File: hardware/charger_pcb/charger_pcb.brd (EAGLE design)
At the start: 60 x 30 mm, 17 parts

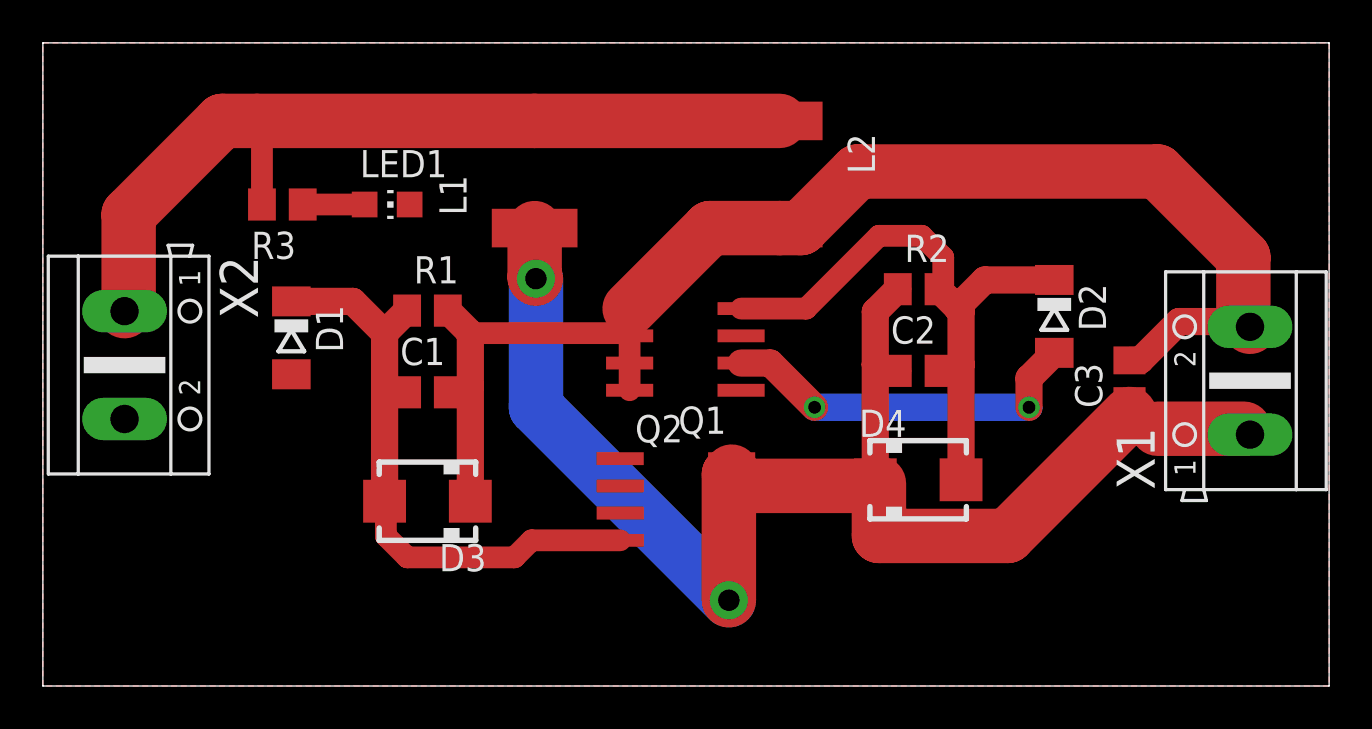
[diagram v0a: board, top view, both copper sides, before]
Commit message: better dir struct, and some tweaks to pcbs
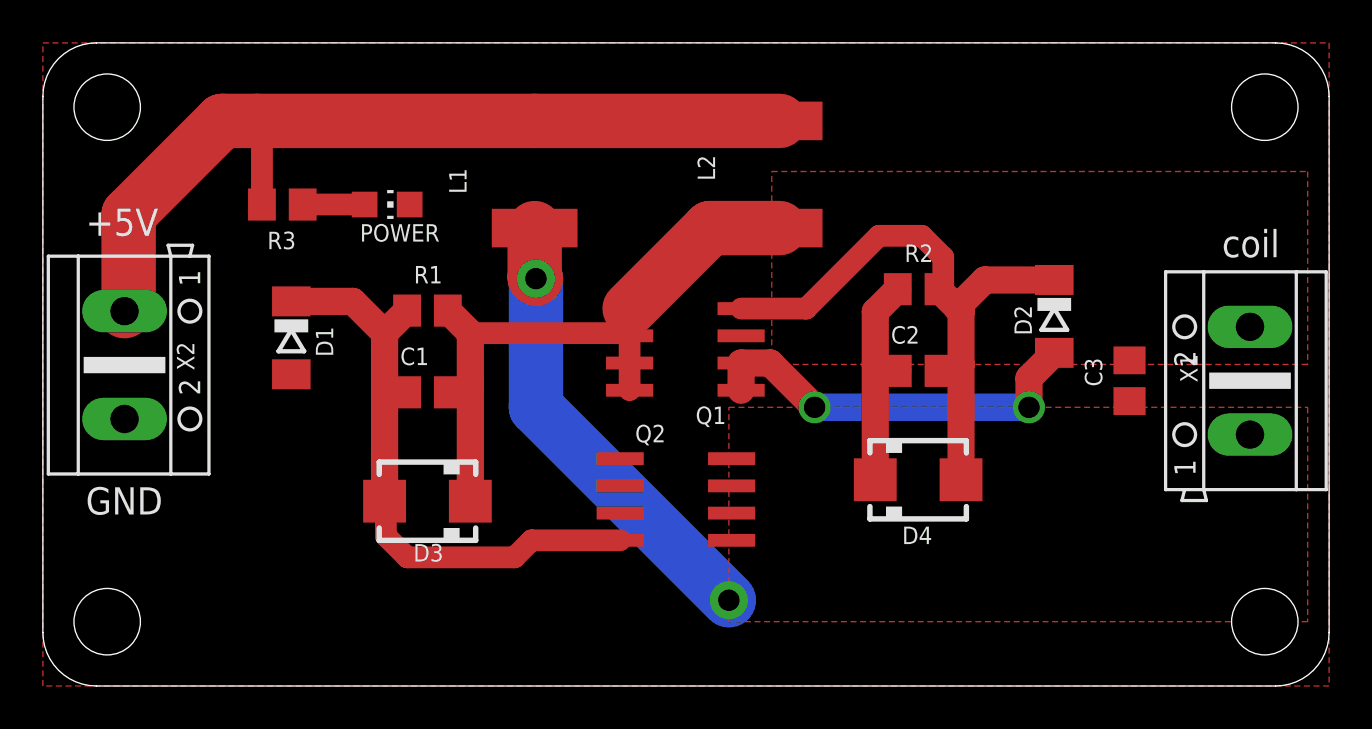
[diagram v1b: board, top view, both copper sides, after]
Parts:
- renumbered LED1 to POWER
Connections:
- net N$2 renamed OUT1
- net N$4 renamed OUT2
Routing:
- net OUT2: track 71.7 -> 32.4 mm
- net OUT1: track 68.2 -> 34.0 mm
- net GND: track 17.3 -> 18.6 mm
- added copper zone on layer 1, net OUT1
- added copper zone on layer 1, net OUT2
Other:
- outline, holes or cut-outs redrawn
- board text added: "+5V"
- board text added: "GND"
- board text added: "coil"

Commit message: checkpoints revised with Matt, new footprints
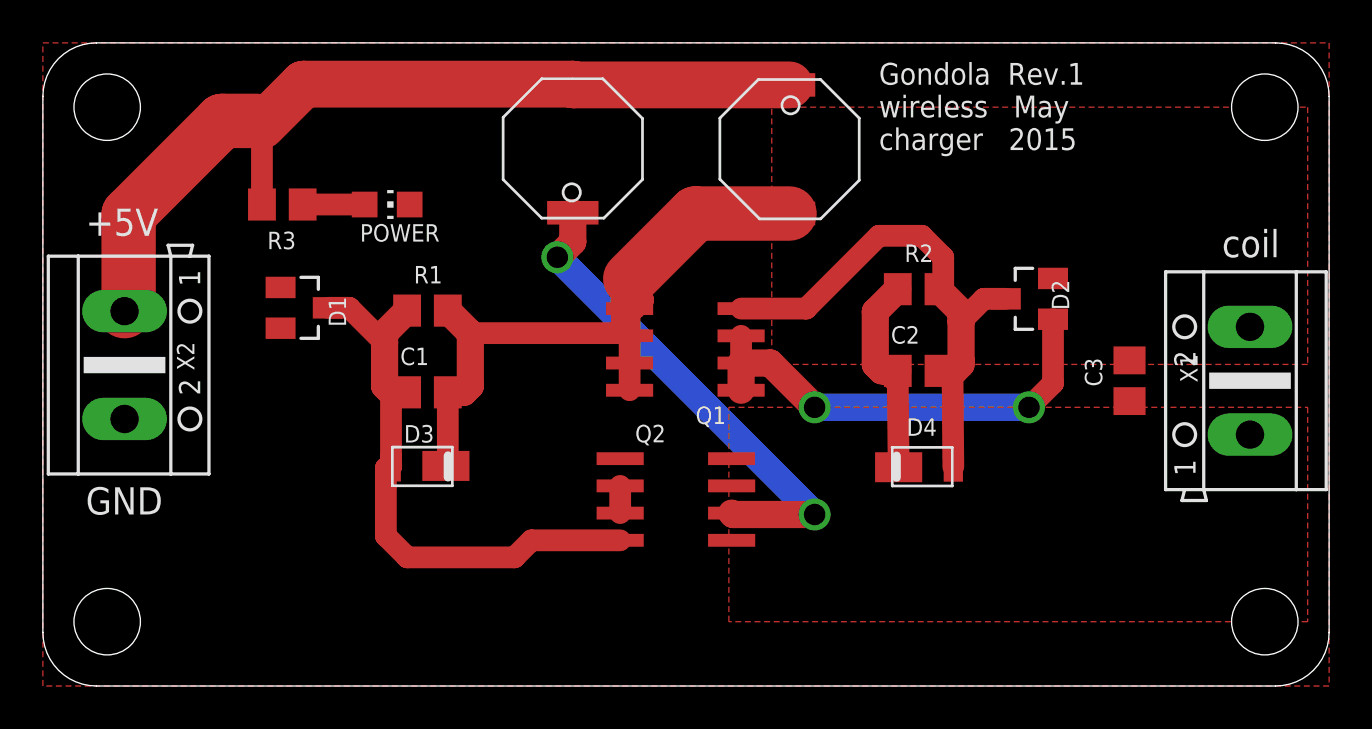
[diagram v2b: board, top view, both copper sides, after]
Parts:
- removed L1, L2: 68uH, rcl:L5650M
- added U$1, U$2: SRU6018, custom parts:SRU6018
- D1, D2: device diode:SOD80C -> diode:SOT23
- D3, D4: value 40V2A -> DFLS240L; device diode:SMA -> custom parts:POWERDI123
- moved D3 1.64 mm to (17.7, 10.2)
- moved D1 1.52 mm to (12.2, 17.6)
- moved D2 1.42 mm to (46.0, 18.1), turned to 90 degrees
- moved D4 0.64 mm to (41.0, 10.2)
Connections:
- net +5V: now also U$1.P$1, U$2.P$2; no longer L1.2, L2.1
- net GND: now also D1.1, D2.1; no longer D1.A, D2.A
- net N$1: now also D1.3; no longer D1.C
- net N$3: now also D2.3; no longer D2.C
- net OUT1: now also D3.K, U$2.P$1; no longer D3.C, L2.2
- net OUT2: now also D4.K, U$1.P$2; no longer D4.C, L1.1
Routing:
- net GND: track 18.6 -> 22.7 mm
- net N$3: track 28.4 -> 25.6 mm
- net N$1: track 28.8 -> 27.0 mm
- net OUT2: track 32.4 -> 33.5 mm
- net +5V: track 40.8 -> 41.8 mm
- net OUT1: track 34.0 -> 33.3 mm
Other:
- board text added: "Gondola Rev.1 wireless May charger 2015"
